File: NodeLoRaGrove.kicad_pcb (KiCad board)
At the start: 2 copper layers, 40 x 50 mm, 43 parts, among them P1 PICKIT PROGRAMMER, P2 ICSP, P3 USB_A, P4 - Battery +, P5 A0, P6 D9, P7 I2C, P8 A2, SW1 RESET, U1 AP2112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

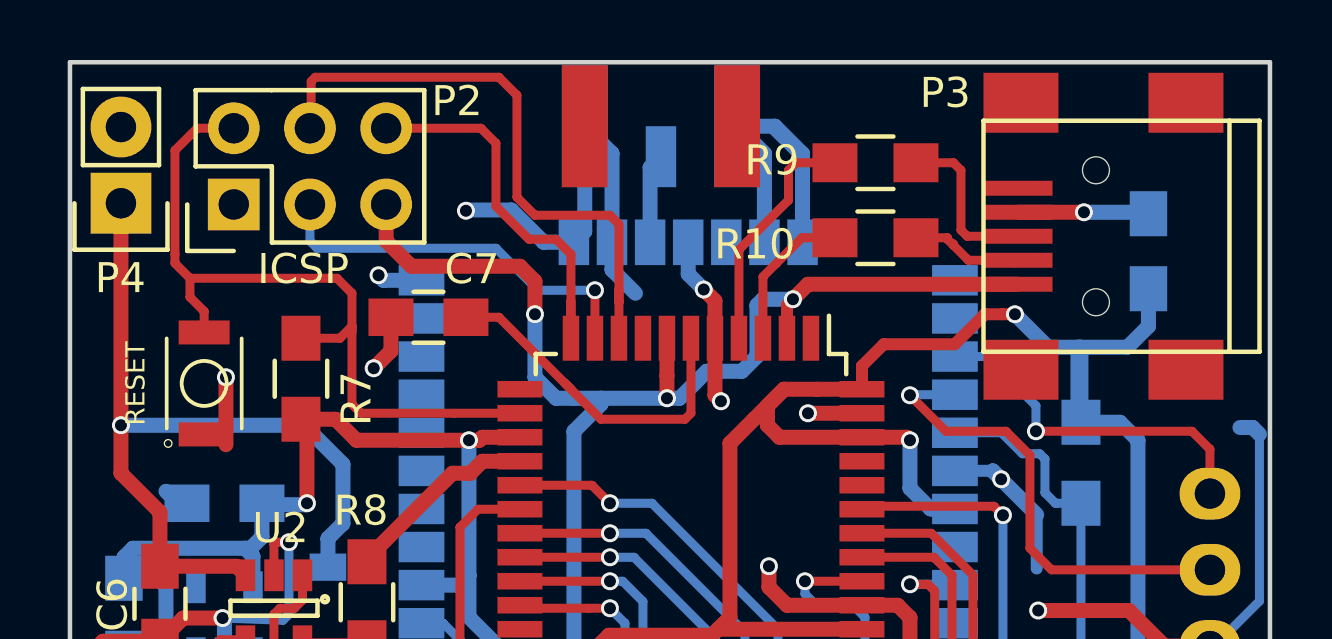
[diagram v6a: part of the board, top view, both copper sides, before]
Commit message: Change USB connector
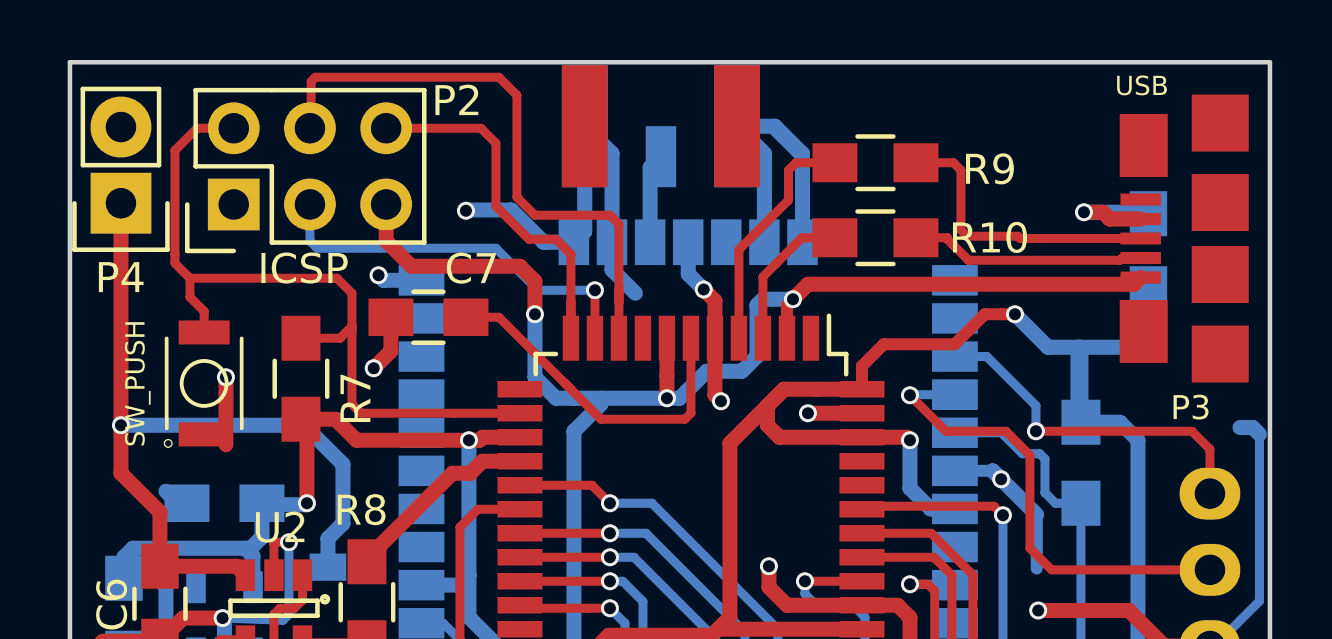
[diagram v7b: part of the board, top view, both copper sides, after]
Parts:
- P3: value USB_A -> USB; footprint Connect:USB_Mini-B -> TIH:10118192-0001LF
- P4: value - Battery + -> Battery
- SW1: value RESET -> SW_PUSH
- moved P3 4.74 mm to (164.6, 81.0), turned to 90 degrees
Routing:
- net VCC: track 157.8 -> 162.0 mm
- net /D+: track 5.58 -> 9.71 mm
- net /D-: track 3.93 -> 7.91 mm

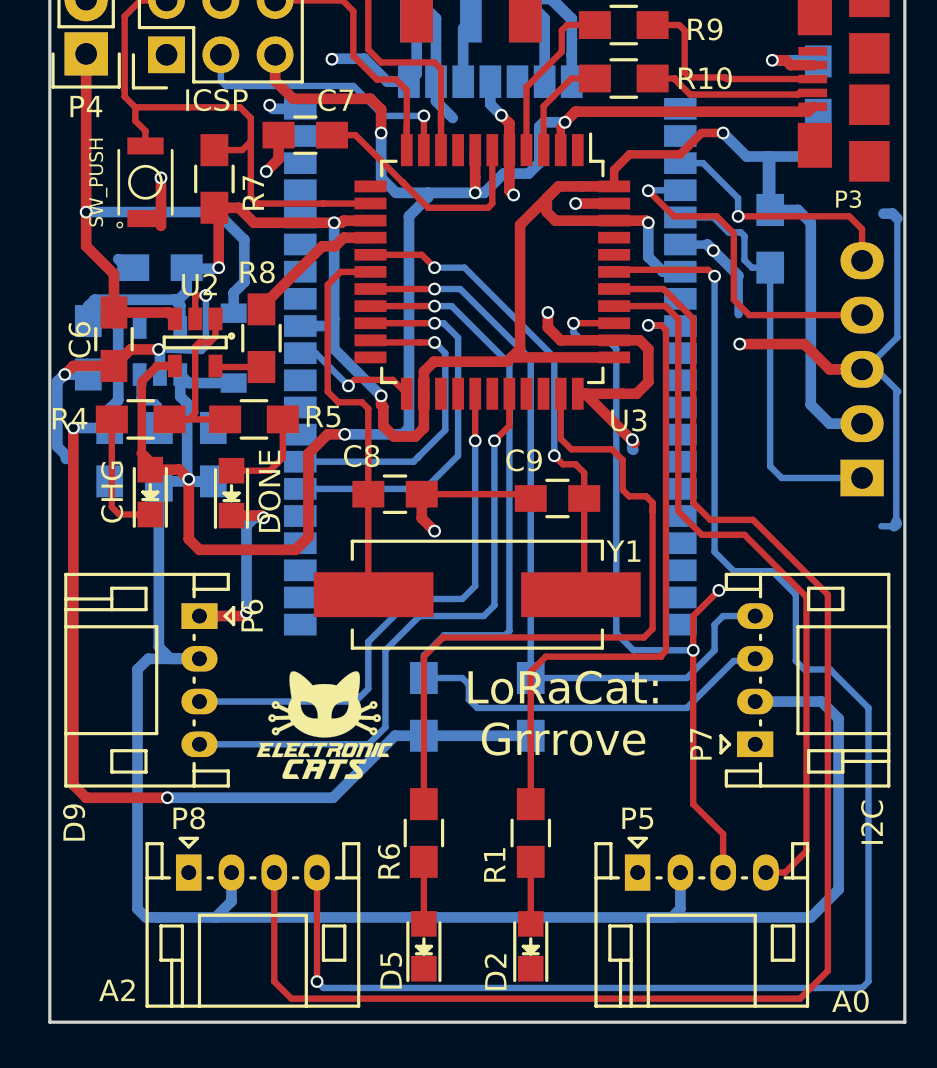
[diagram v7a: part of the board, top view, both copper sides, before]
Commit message: Update logos
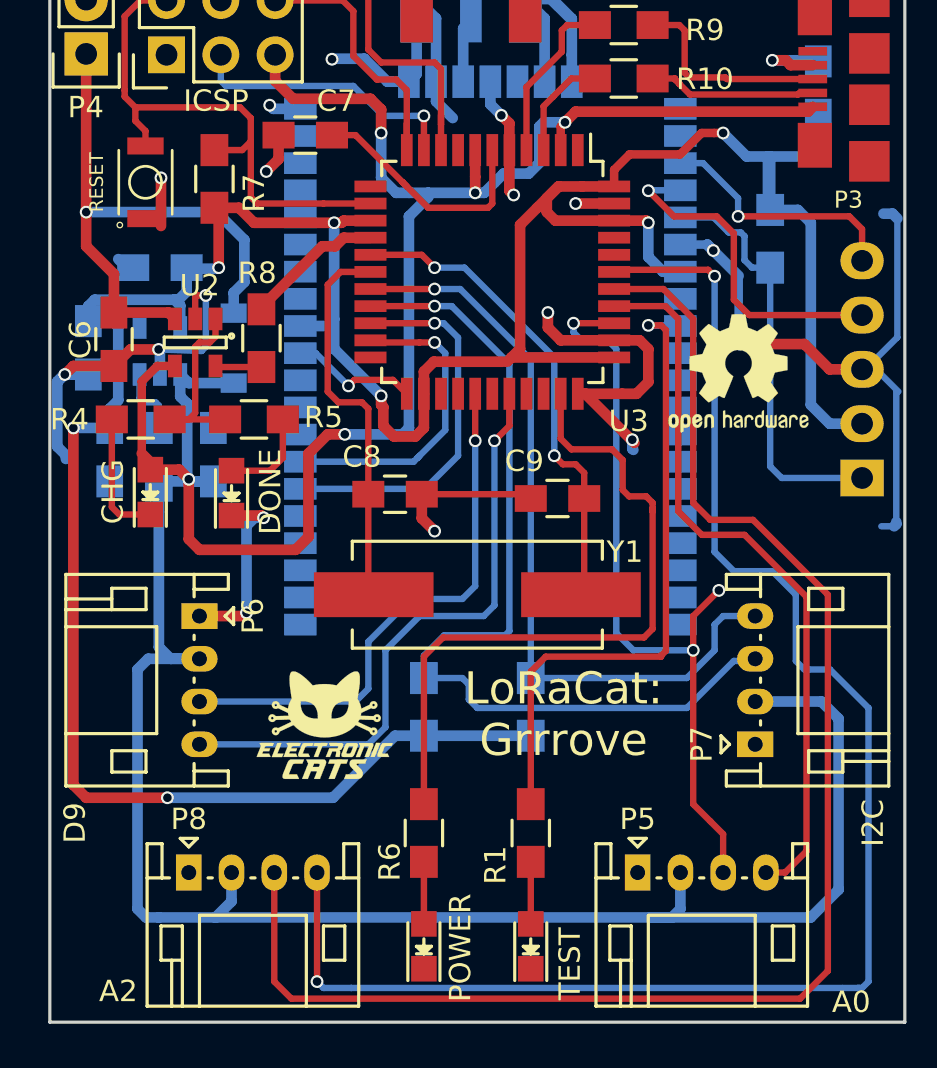
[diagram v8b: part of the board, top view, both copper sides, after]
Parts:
- added REF***: FCC-Logo_7.3x6mm_SilkScreen, Symbols:FCC-Logo_7.3x6mm_SilkScreen, B.Cu at (144.9, 119.9)
- D2: value Led -> TEST
- D5: value LED -> POWER
- P4: value Battery -> - Battery +
- REF***: moved to F.Cu
- SW1: value SW_PUSH -> RESET
- moved REF*** 26.6 mm to (157.0, 94.8), turned to 0 degrees
